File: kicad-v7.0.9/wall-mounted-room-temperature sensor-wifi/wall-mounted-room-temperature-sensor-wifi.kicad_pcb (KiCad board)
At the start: 2 copper layers, 107 x 90 mm, 61 parts, among them J1 PC-GK2.1, P1 2x3_MLW06A, P2 DS1023-1-9S21, Q1 DMG2307L, SW1 TVAF18BB, SW2 TVAF18BB, SW3 B3F-4150, SW4 B3F-4150, SW5 B3F-4150, U1 TPS79633KTTR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

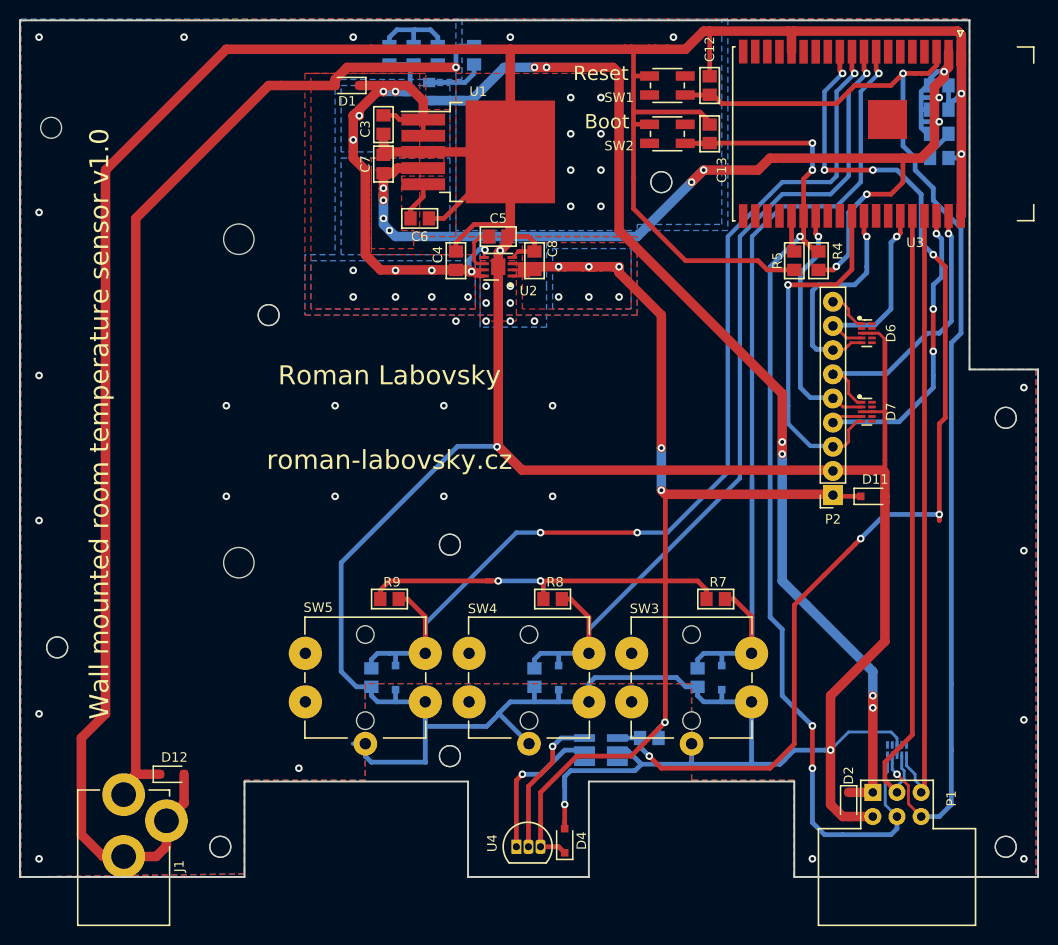
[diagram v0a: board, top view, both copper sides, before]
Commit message: Change components form library. Adding of BOM.
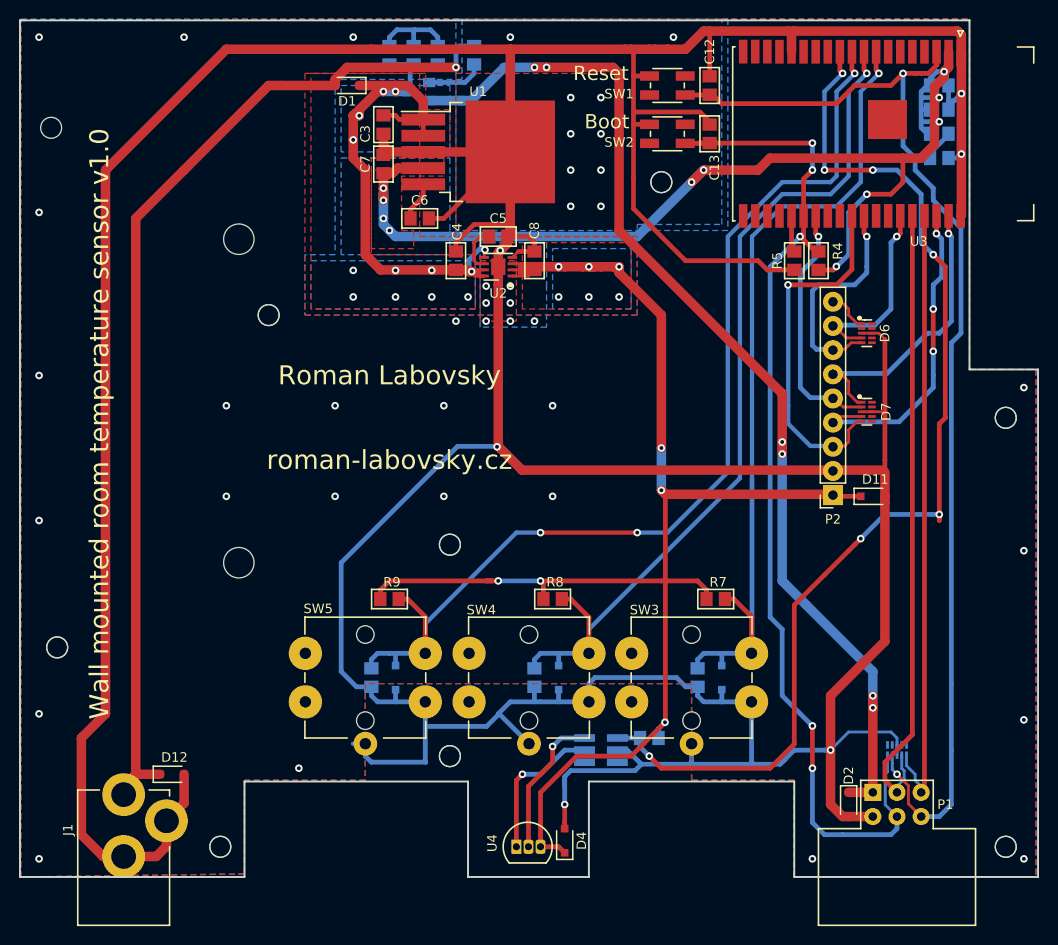
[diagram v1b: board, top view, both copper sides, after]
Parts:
- P1: footprint connector_idc_rl:2x3_MLW06A -> connector_idc_tht_rl:2x3_MLW06A
- P2: footprint connector_tht_pinsocket_2.54mm_rl:1x9_pinsocket_2.54mm_vertical_8.5mm -> connector_pin_socket_2.54mm_tht_rl:1x9_pin_socket_2.54mm_vertical_8.5mm
